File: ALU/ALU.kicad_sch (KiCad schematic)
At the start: 26 parts, among them J1 Conn_01x06_Pin, J2 Conn_01x08_Pin, J3 Conn_01x08_Pin, J4 Conn_01x10_Pin, U1 SN74F86N, U2 SN74F86N, U3 SN74HCT245N, U4 CD74HCT283E, U5 CD74HCT283E

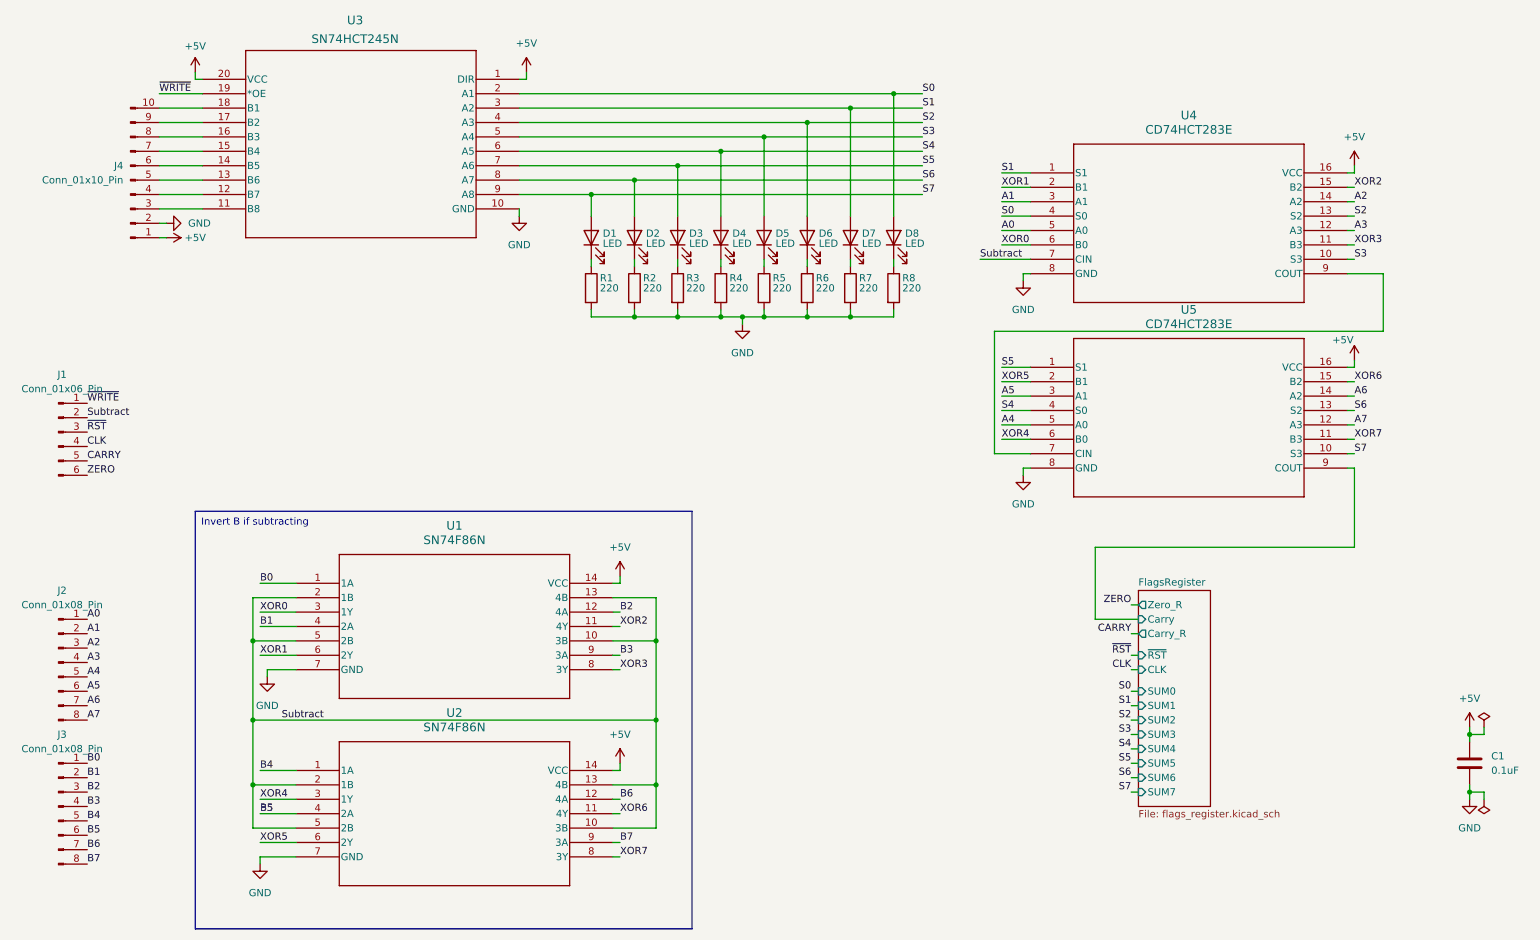
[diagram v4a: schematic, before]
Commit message: Forgot Flags register input enable. Passing clock though spare AND gate with new input Flag In input to create equvilant
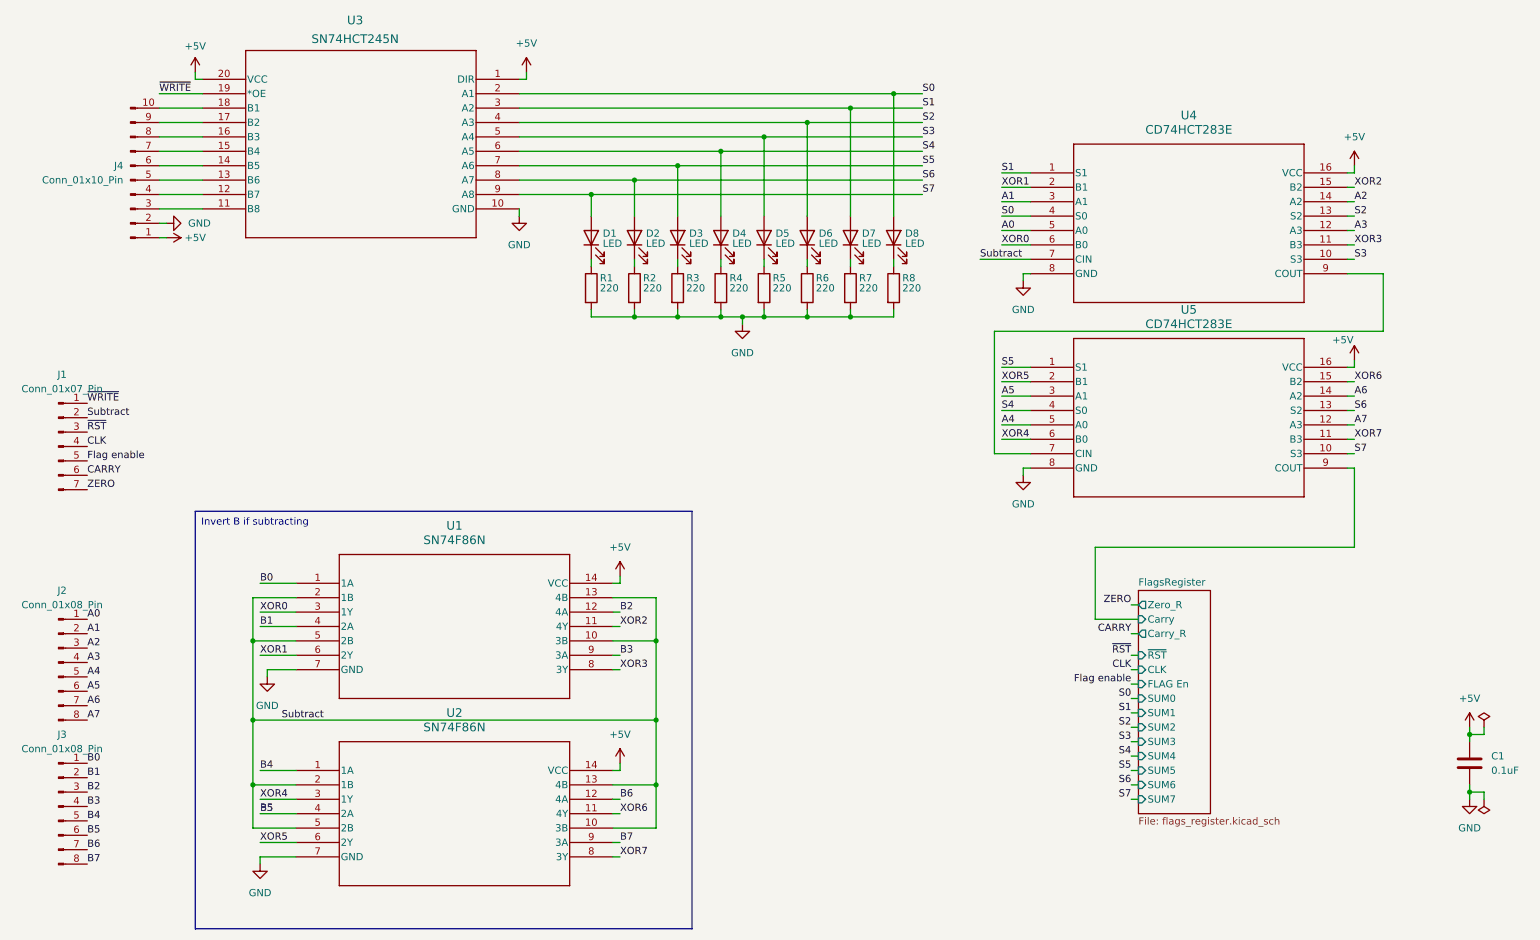
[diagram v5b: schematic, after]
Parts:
- removed J1: Conn_01x06_Pin, Connector_PinHeader_2.54mm:PinHeader_1x06_P2.54mm_Vertical, symbol Connector:Conn_01x06_Pin
- added J1: Conn_01x07_Pin, Connector_PinHeader_2.54mm:PinHeader_1x07_P2.54mm_Vertical, symbol Connector:Conn_01x07_Pin
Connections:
- net CARRY: now also J1.6 (Pin_6)
- net CLK: now also J1.4 (Pin_4)
- net Subtract: now also J1.2 (Pin_2)
- net ZERO: now also J1.7 (Pin_7)
- net ~{RST}: now also J1.3 (Pin_3)
- net ~{WRITE}: now also J1.1 (Pin_1)
- new net Flag enable: J1.5 (Pin_5)
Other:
- sheet FlagsRegister ports: added FLAG En; removed none
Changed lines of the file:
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@@
 	(wire
 		(pts
-			(xy 209.55 151.13) (xy 210.82 151.13)
+			(xy 209.55 152.4) (xy 210.82 152.4)
 		)
 		(stroke
@@
 	(wire
 		(pts
-			(xy 209.55 135.89) (xy 210.82 135.89)
+			(xy 209.55 137.16) (xy 210.82 137.16)
 		)
 		(stroke
@@
 	(wire
 		(pts
-			(xy 209.55 138.43) (xy 210.82 138.43)
+			(xy 209.55 139.7) (xy 210.82 139.7)
 		)
 		(stroke
@@
 	(wire
 		(pts
-			(xy 209.55 148.59) (xy 210.82 148.59)
+			(xy 209.55 149.86) (xy 210.82 149.86)
 		)
 		(stroke
@@
 	(wire
 		(pts
-			(xy 209.55 133.35) (xy 210.82 133.35)
+			(xy 209.55 134.62) (xy 210.82 134.62)
 		)
 		(stroke
@@
 	(wire
 		(pts
-			(xy 209.55 146.05) (xy 210.82 146.05)
+			(xy 209.55 147.32) (xy 210.82 147.32)
+		)
+		(stroke
+			(width 0)
+			(type default)
+		)
+	)
+	(wire
+		(pts
+			(xy 209.55 132.08) (xy 210.82 132.08)
 		)
 		(stroke
@@
 	(wire
 		(pts
-			(xy 209.55 143.51) (xy 210.82 143.51)
+			(xy 209.55 144.78) (xy 210.82 144.78)
 		)
 		(stroke
@@
 	(wire
 		(pts
-			(xy 209.55 140.97) (xy 210.82 140.97)
+			(xy 209.55 142.24) (xy 210.82 142.24)
 		)
 		(stroke
@@
 	)
 	(label "S2"
-		(at 209.55 138.43 180)
+		(at 209.55 139.7 180)
 		(fields_autoplaced yes)
 		(effects
@@
 	)
 	(label "S0"
-		(at 209.55 133.35 180)
+		(at 209.55 134.62 180)
 		(fields_autoplaced yes)
 		(effects
@@
 	)
 	(label "S1"
-		(at 209.55 135.89 180)
+		(at 209.55 137.16 180)
 		(fields_autoplaced yes)
 		(effects
@@
 	)
 	(label "S7"
-		(at 209.55 151.13 180)
+		(at 209.55 152.4 180)
 		(fields_autoplaced yes)
 		(effects
@@
 	)
 	(label "ZERO"
-		(at 25.4 95.25 0)
+		(at 25.4 97.79 0)
 		(fields_autoplaced yes)
 		(effects
@@
 	)
 	(label "S4"
-		(at 209.55 143.51 180)
+		(at 209.55 144.78 180)
 		(fields_autoplaced yes)
 		(effects
@@
 	)
 	(label "S6"
-		(at 209.55 148.59 180)
+		(at 209.55 149.86 180)
 		(fields_autoplaced yes)
 		(effects
@@
 	)
 	(label "CARRY"
-		(at 25.4 92.71 0)
+		(at 25.4 95.25 0)
 		(fields_autoplaced yes)
 		(effects
@@
 		)
 	)
+	(label "Flag enable"
+		(at 25.4 92.71 0)
+		(fields_autoplaced yes)
+		(effects
+			(font
+				(size 1.27 1.27)
+			)
+			(justify left bottom)
+		)
+	)
+	(label "Flag enable"
+		(at 209.55 132.08 180)
+		(fields_autoplaced yes)
+		(effects
+			(font
+				(size 1.27 1.27)
+			)
+			(justify right bottom)
+		)
+	)
 	(label "A5"
 		(at 25.4 133.35 0)
@@
 	)
 	(label "S3"
-		(at 209.55 140.97 180)
+		(at 209.55 142.24 180)
 		(fields_autoplaced yes)
 		(effects
@@
 	)
 	(label "S5"
-		(at 209.55 146.05 180)
+		(at 209.55 147.32 180)
 		(fields_autoplaced yes)
 		(effects
@@
 	)
 	(symbol
+		(lib_id "Connector:Conn_01x07_Pin")
+		(at 20.32 90.17 0)
+		(unit 1)
+		(exclude_from_sim no)
+		(in_bom yes)
+		(on_board yes)
+		(dnp no)
+		(fields_autoplaced yes)
+		(property "Reference" "J1"
+			(at 20.955 77.47 0)
+			(effects
+				(font
+					(size 1.27 1.27)
+				)
+			)
+		)
+		(property "Value" "Conn_01x07_Pin"
+			(at 20.955 80.01 0)
+			(effects
+				(font
+					(size 1.27 1.27)
+				)
+			)
+		)
+		(property "Footprint" "Connector_PinHeader_2.54mm:PinHeader_1x07_P2.54mm_Vertical"
+			(at 20.32 90.17 0)
+			(effects
+				(font
+					(size 1.27 1.27)
+				)
+				(hide yes)
+			)
+		)
+		(property "Datasheet" "~"
+			(at 20.32 90.17 0)
+			(effects
+				(font
+					(size 1.27 1.27)
+				)
+				(hide yes)
+			)
+		)
+		(property "Description" "Generic connector, single row, 01x07, script generated"
+			(at 20.32 90.17 0)
+			(effects
+				(font
+					(size 1.27 1.27)
+				)
+				(hide yes)
+			)
+		)
+		(pin "1"
+		)
+		(pin "4"
+		)
+		(pin "3"
+		)
+		(pin "2"
+		)
+		(pin "6"
+		)
+		(pin "7"
+		)
+		(pin "5"
+		)
+		(instances
+			(project ""
+				(path "/62101b97-a334-4edf-8cb6-c85e816b5b90"
+					(reference "J1")
+					(unit 1)
+				)
+			)
+		)
+	)
+	(symbol
 		(lib_id "power:+5V")
 		(at 119.38 113.03 0)
@@
 	)
 	(symbol
-		(lib_id "Connector:Conn_01x06_Pin")
-		(at 20.32 87.63 0)
-		(unit 1)
-		(exclude_from_sim no)
-		(in_bom yes)
-		(on_board yes)
-		(dnp no)
-		(fields_autoplaced yes)
-		(property "Reference" "J1"
-			(at 20.955 77.47 0)
-			(effects
-				(font
-					(size 1.27 1.27)
-				)
-			)
-		)
-		(property "Value" "Conn_01x06_Pin"
-			(at 20.955 80.01 0)
-			(effects
-				(font
-					(size 1.27 1.27)
-				)
-			)
-		)
-		(property "Footprint" "Connector_PinHeader_2.54mm:PinHeader_1x06_P2.54mm_Vertical"
-			(at 20.32 87.63 0)
-			(effects
-				(font
-					(size 1.27 1.27)
-				)
-				(hide yes)
-			)
-		)
-		(property "Datasheet" "~"
-			(at 20.32 87.63 0)
-			(effects
-				(font
-					(size 1.27 1.27)
-				)
-				(hide yes)
-			)
-		)
-		(property "Description" "Generic connector, single row, 01x06, script generated"
-			(at 20.32 87.63 0)
-			(effects
-				(font
-					(size 1.27 1.27)
-				)
-				(hide yes)
-			)
-		)
-		(pin "1"
-		)
-		(pin "5"
-		)
-		(pin "6"
-		)
-		(pin "2"
-		)
-		(pin "4"
-		)
-		(pin "3"
-		)
-		(instances
-			(project ""
-				(path "/62101b97-a334-4edf-8cb6-c85e816b5b90"
-					(reference "J1")
-					(unit 1)
-				)
-			)
-		)
-	)
-	(symbol
 		(lib_id "power:+5V")
 		(at 119.38 146.05 0)
@@
 	(sheet
 		(at 210.82 115.57)
-		(size 12.7 38.1)
+		(size 12.7 39.37)
 		(fields_autoplaced yes)
 		(stroke
@@
 		)
 		(property "Sheetfile" "flags_register.kicad_sch"
-			(at 210.82 154.2546 0)
+			(at 210.82 155.5246 0)
 			(effects
 				(font
@@
 		)
 		(pin "SUM1" input
-			(at 210.82 135.89 180)
+			(at 210.82 137.16 180)
 			(effects
 				(font
@@
 		)
 		(pin "SUM2" input
-			(at 210.82 138.43 180)
+			(at 210.82 139.7 180)
 			(effects
 				(font
@@
 		)
 		(pin "SUM0" input
-			(at 210.82 133.35 180)
+			(at 210.82 134.62 180)
 			(effects
 				(font
@@
 		)
 		(pin "SUM7" input
-			(at 210.82 151.13 180)
+			(at 210.82 152.4 180)
 			(effects
 				(font
@@
 		)
 		(pin "SUM6" input
-			(at 210.82 148.59 180)
+			(at 210.82 149.86 180)
 			(effects
 				(font
@@
 		)
 		(pin "SUM4" input
-			(at 210.82 143.51 180)
+			(at 210.82 144.78 180)
 			(effects
 				(font
@@
 		)
 		(pin "SUM5" input
-			(at 210.82 146.05 180)
+			(at 210.82 147.32 180)
 			(effects
 				(font
@@
 		)
 		(pin "SUM3" input
-			(at 210.82 140.97 180)
+			(at 210.82 142.24 180)
+			(effects
+				(font
+					(size 1.27 1.27)
+				)
+				(justify left)
+			)
+		)
+		(pin "FLAG En" input
+			(at 210.82 132.08 180)
 			(effects
 				(font
